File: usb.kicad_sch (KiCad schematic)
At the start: 87 parts, among them J3 PinHeader_1x3_P2.54mm_Drill1.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, J4 USB-C_Amphenol_12401598E4, J5 USB-C_Amphenol_12401598E4, J6 USB-C_Amphenol_12401598E4, U16 AP7366_SOT, U17 HD3SS3220IRNHR, U18 TPD4E05U06QDQARQ1, U19 TPD4E05U06QDQARQ1, U20 TPD4E05U06QDQARQ1, U21 USB7252C, U22 W25Q80DV_USON, U23 TPD4E05U06QDQARQ1, U24 TPD4E05U06QDQARQ1, U25 TPD4E05U06QDQARQ1, U26 TPD4E05U06QDQARQ1, U27 TPD4E05U06QDQARQ1, U28 TPD4E05U06QDQARQ1, Y2 Oscillator_25MHz_ESC_2016MV

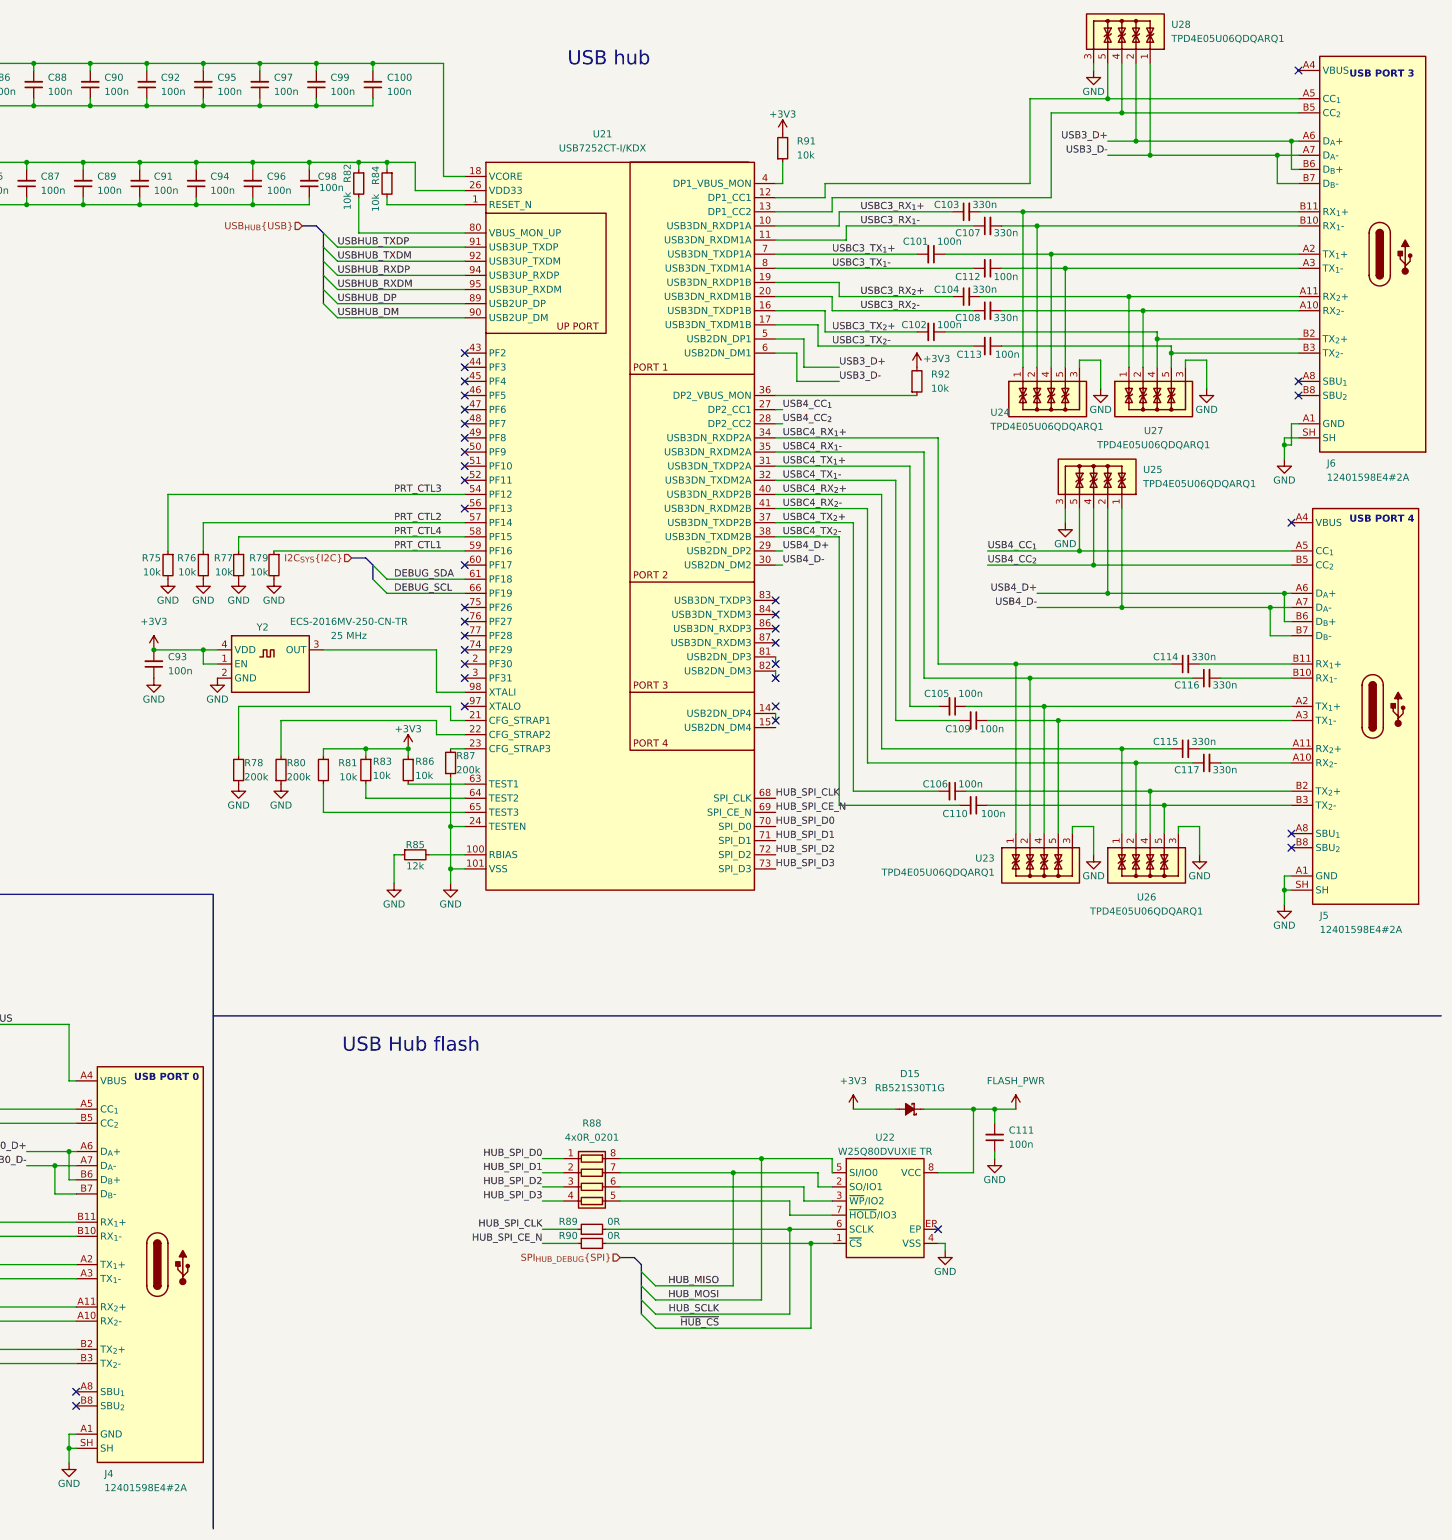
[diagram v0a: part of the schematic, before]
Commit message: [#82847] Prepare current state of schematic to merge with mockup
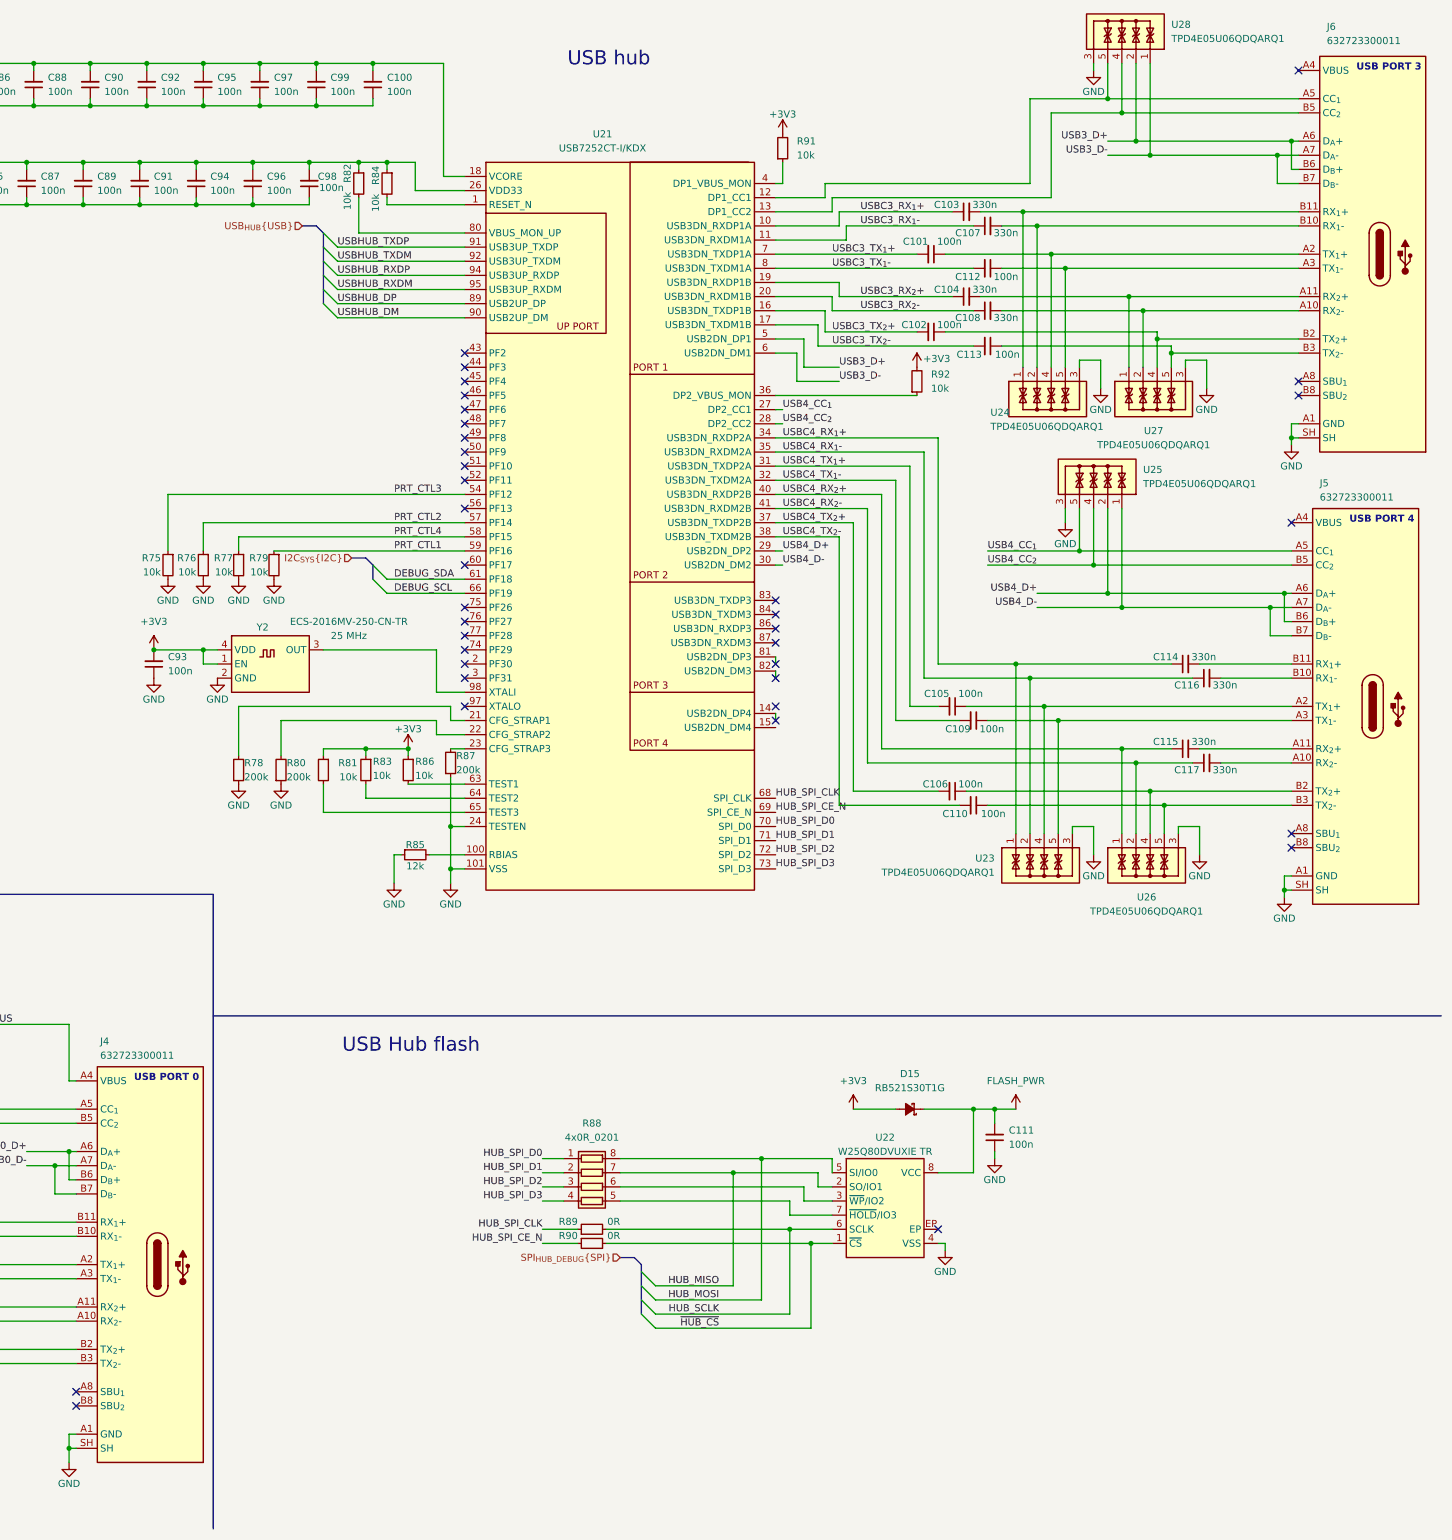
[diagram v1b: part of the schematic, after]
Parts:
- removed J4, J5, J6: USB-C_Amphenol_12401598E4, antmicro-footprints:USB-C_Receptacle_Amphenol_12401598E4, symbol antmicroUSBConnectors:USB-C_Amphenol_12401598E4
- added J4, J5, J6: USB-C_WE_632723300011, antmicro-footprints:USB-C_Receptacle_WE_632723300011, symbol antmicroUSBConnectors:USB-C_WE_632723300011
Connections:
- net GND: now also J4.A1 (GND), J4.A12 (GND), J4.B1 (GND), J4.B12 (GND), J4.SH, J5.A1 (GND), J5.A12 (GND), J5.B1 (GND), J5.B12 (GND), J5.SH, J6.A1 (GND), J6.A12 (GND), J6.B1 (GND), J6.B12 (GND), J6.SH
- net USB0_D+: now also J4.A6 (D_{A}+), J4.B6 (D_{B}+)
- net USB0_D-: now also J4.A7 (D_{A}-), J4.B7 (D_{B}-)
- net USB0_VBUS: now also J4.A4 (VBUS), J4.A9 (VBUS), J4.B4 (VBUS), J4.B9 (VBUS)
- net USB3_D+: now also J6.A6 (D_{A}+), J6.B6 (D_{B}+)
- net USB3_D-: now also J6.A7 (D_{A}-), J6.B7 (D_{B}-)
- net USB4_CC_{1}: now also J5.A5 (CC_{1})
- net USB4_CC_{2}: now also J5.B5 (CC_{2})
- net USB4_D+: now also J5.A6 (D_{A}+), J5.B6 (D_{B}+)
- net USB4_D-: now also J5.A7 (D_{A}-), J5.B7 (D_{B}-)
- net at C116.2: now also J5.B10 (RX_{1}-)
- net at C115.2: now also J5.A11 (RX_{2}+)
- net at U17.1 (CC2), U19.2, U19.9: now also J4.B5 (CC_{2})
- net at U17.2 (CC1), U19.4, U19.7: now also J4.A5 (CC_{1})
- net at C108.2, U27.2, U27.9: now also J6.A10 (RX_{2}-)
- net at U21.12 (DP1_CC1), U28.5, U28.6: now also J6.A5 (CC_{1})
- net at U21.13 (DP1_CC2), U28.4, U28.7: now also J6.B5 (CC_{2})
- net at C103.2, U24.1, U24.10: now also J6.B11 (RX_{1}+)
- net at C101.1, U24.4, U24.7: now also J6.A2 (TX_{1}+)
- net at C102.1, U27.4, U27.7: now also J6.B2 (TX_{2}+)
- net at C110.1, U26.5, U26.6: now also J5.B3 (TX_{2}-)
- net at C109.1, U23.5, U23.6: now also J5.A3 (TX_{1}-)
- net at C104.2, U27.1, U27.10: now also J6.A11 (RX_{2}+)
- net at C112.1, U24.5, U24.6: now also J6.A3 (TX_{1}-)
- net at C80.1, U18.4, U18.7: now also J4.A2 (TX_{1}+)
- net at U17.14 (RX1-), U18.1, U18.10: now also J4.B11 (RX_{1}+)
- net at U17.15 (RX1+), U18.2, U18.9: now also J4.B10 (RX_{1}-)
- net at C82.1, U18.5, U18.6: now also J4.A3 (TX_{1}-)
- net at C105.1, U23.4, U23.7: now also J5.A2 (TX_{1}+)
- net at C117.2: now also J5.A10 (RX_{2}-)
- net at C114.2: now also J5.B11 (RX_{1}+)
- net at C106.1, U26.4, U26.7: now also J5.B2 (TX_{2}+)
- net at U17.18 (RX2-), U20.1, U20.10: now also J4.A11 (RX_{2}+)
- net at U17.19 (RX2+), U20.2, U20.9: now also J4.A10 (RX_{2}-)
- net at C81.1, U20.4, U20.7: now also J4.B2 (TX_{2}+)
- net at C113.1, U27.5, U27.6: now also J6.B3 (TX_{2}-)
- net at C107.2, U24.2, U24.9: now also J6.B10 (RX_{1}-)
- net at C83.1, U20.5, U20.6: now also J4.B3 (TX_{2}-)
- new net: J6.A4 (VBUS), J6.A9 (VBUS), J6.B4 (VBUS), J6.B9 (VBUS)
- new net: J5.A4 (VBUS), J5.A9 (VBUS), J5.B4 (VBUS), J5.B9 (VBUS)

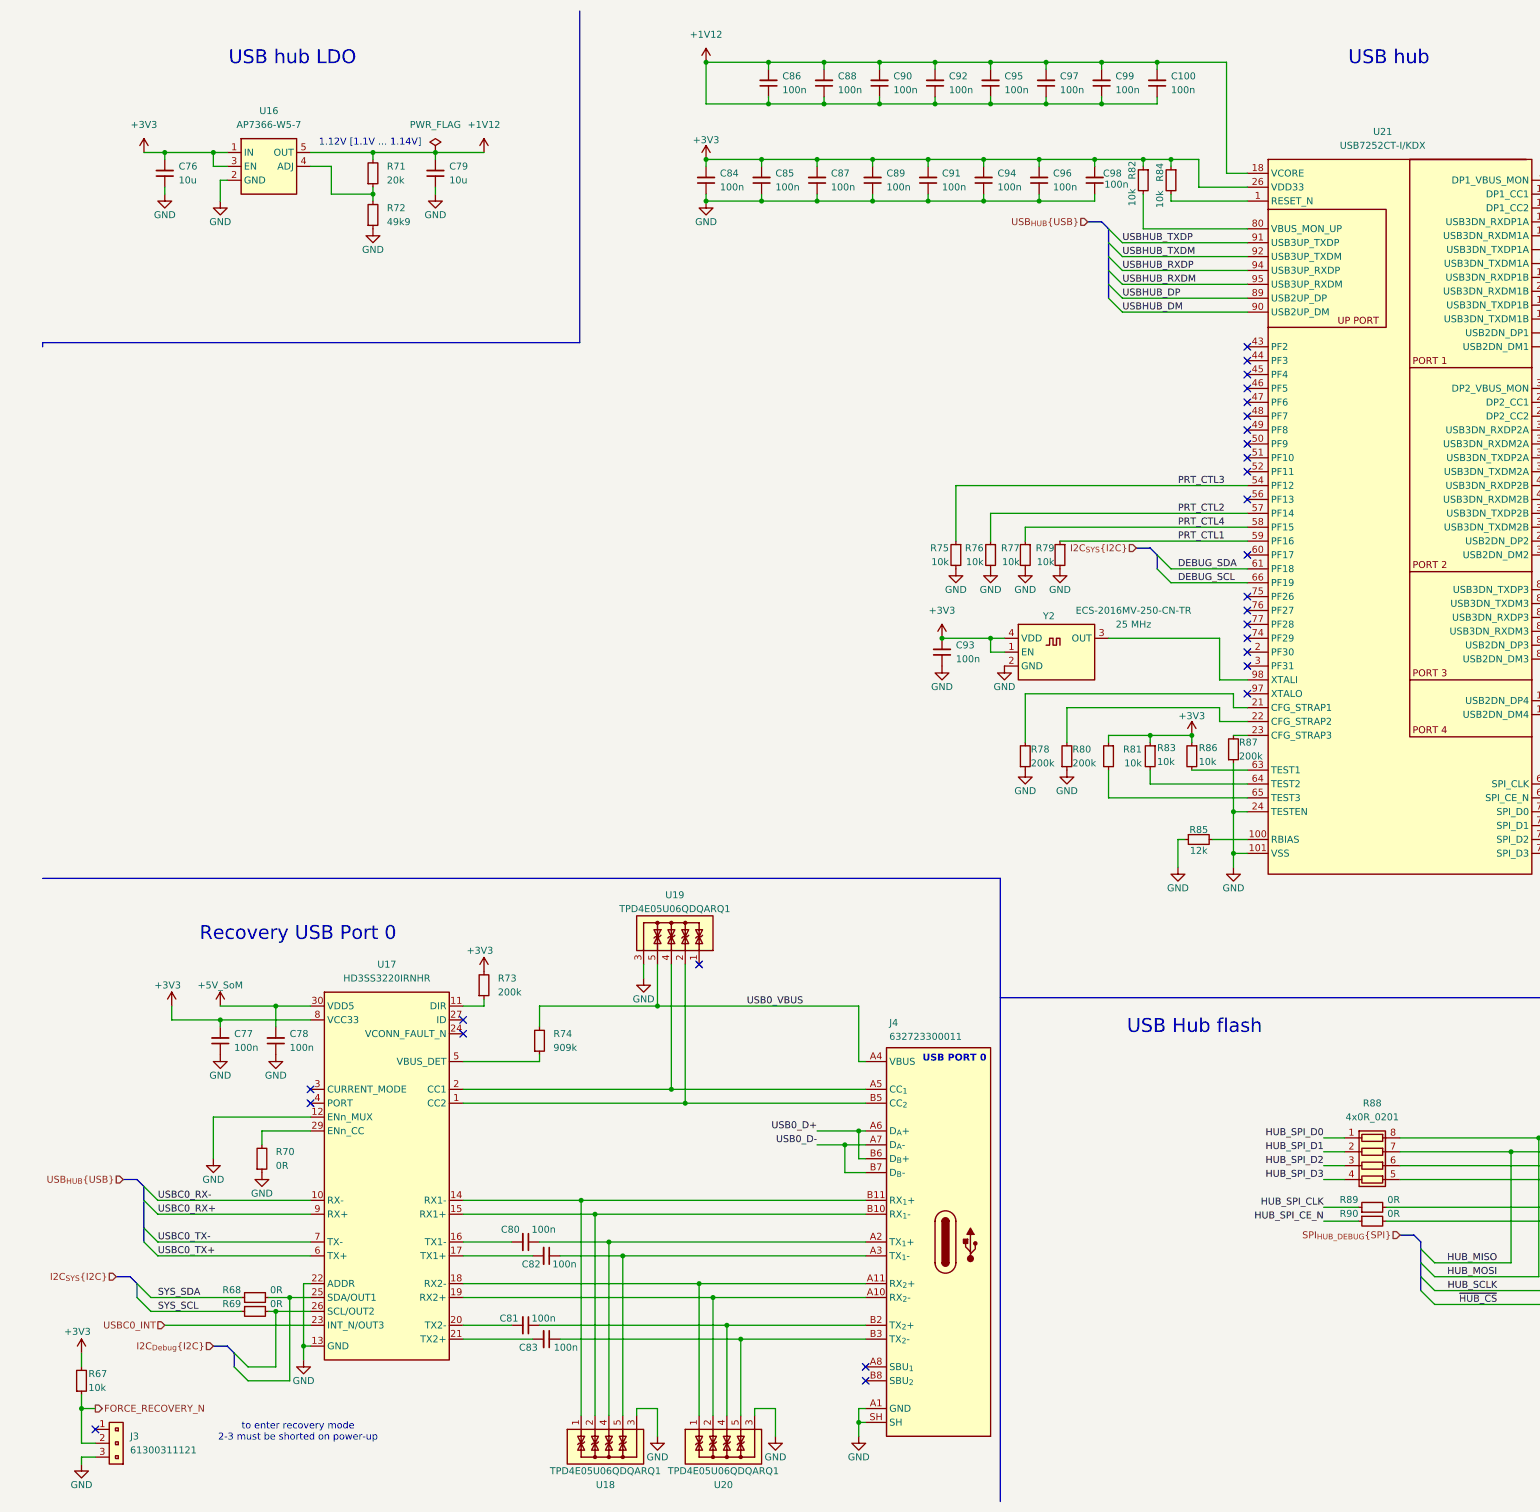
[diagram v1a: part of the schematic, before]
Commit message: [#82837] Standardise sheet sections text size
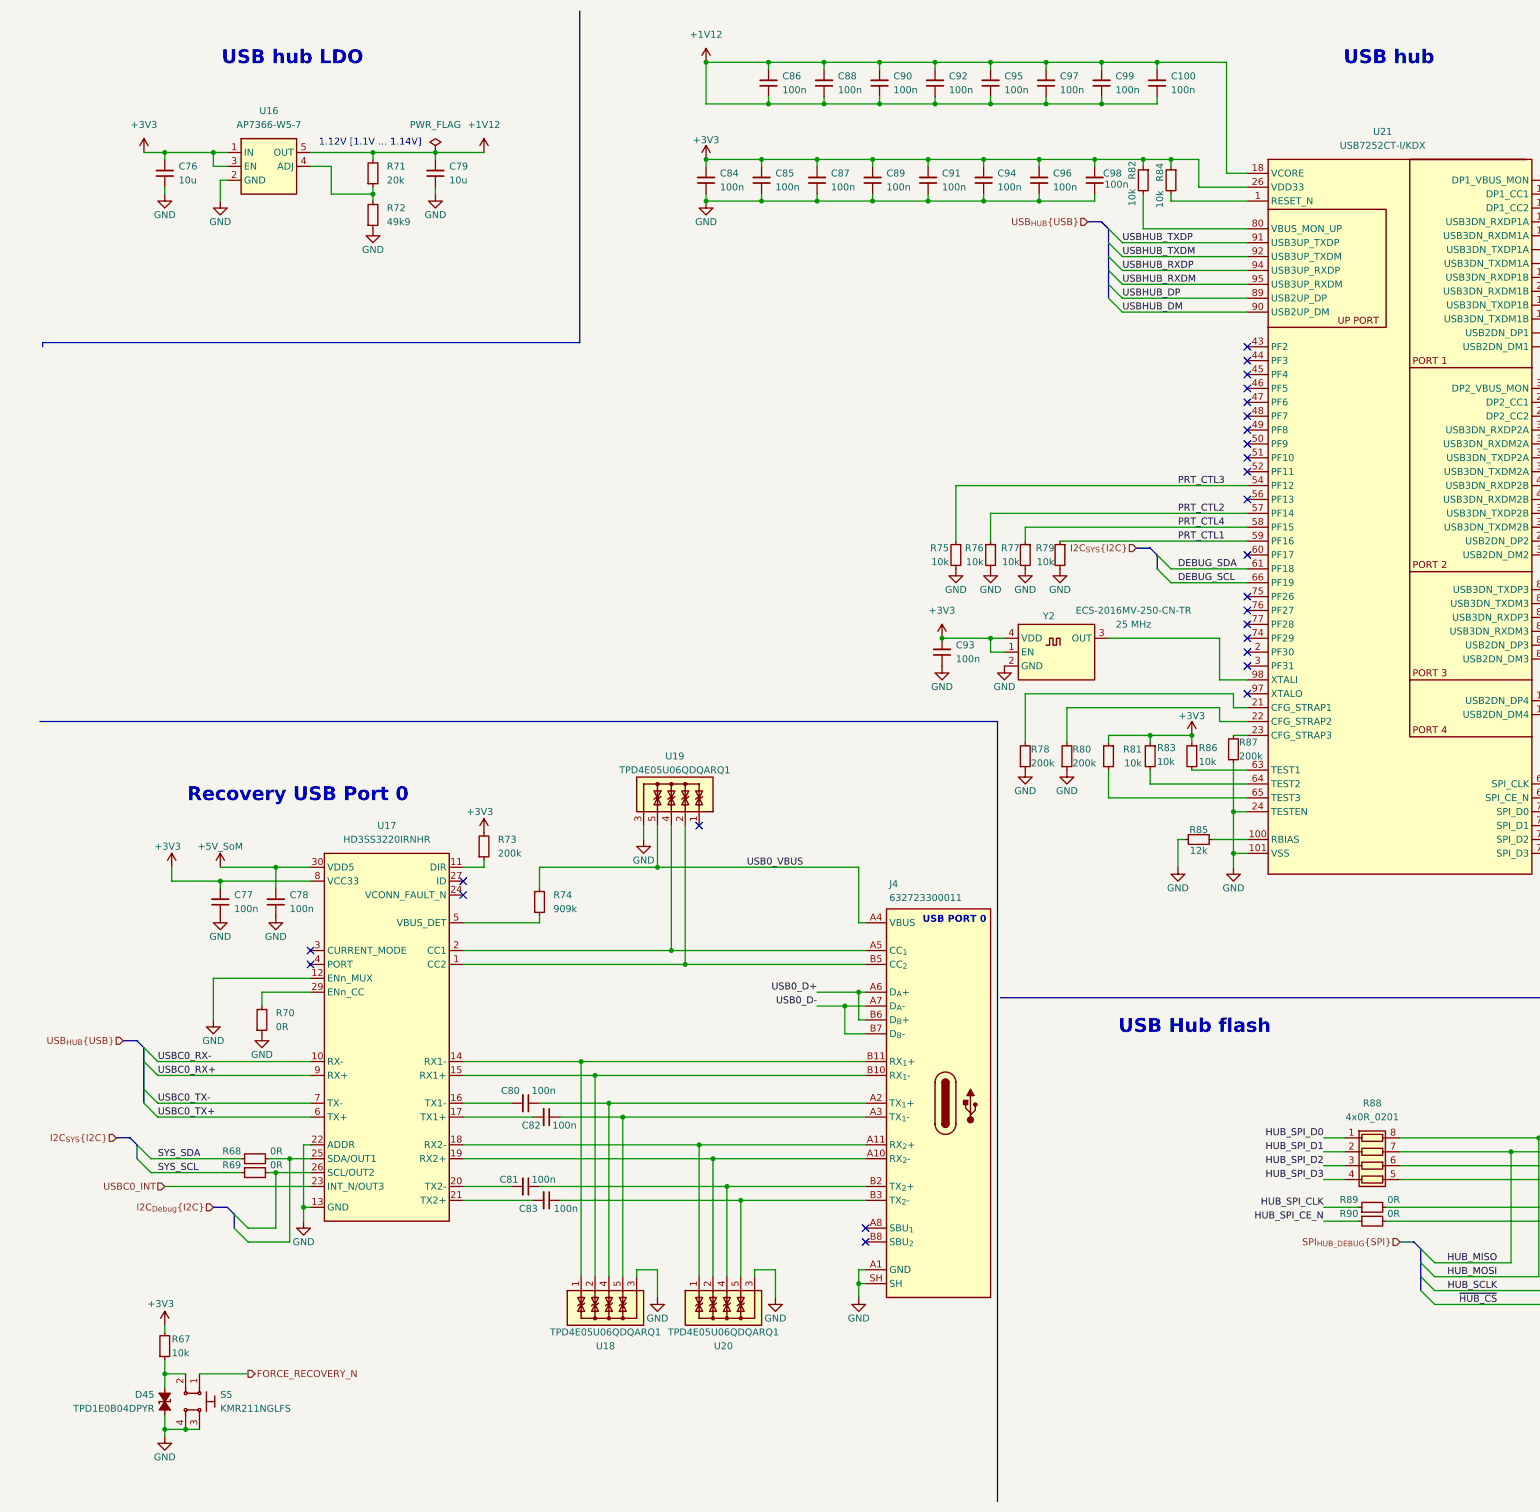
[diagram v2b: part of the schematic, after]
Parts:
- removed J3: PinHeader_1x3_P2.54mm_Drill1.1mm, antmicro-footprints:PinHeader_1x3_P2.54mm_Drill1.1mm, symbol antmicroGenericPinHeaders:PinHeader_1x3_P2.54mm_Drill1.1mm
- added D45: TPD1E0B04_XDFN-2, antmicro-footprints:XDFN-2_1x0.60mm, symbol antmicroTVSDiodes:TPD1E0B04_XDFN-2
- added S5: SW_KMR211NGLFS_SMD, antmicro-footprints:SW_KMR211NGLFS_SMD, symbol antmicroPushbuttonSwitches:SW_KMR211NGLFS_SMD
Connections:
- net FORCE_RECOVERY_N: now also S5.1; no longer R67.1
- net GND: now also D45.1 (C), S5.3, S5.4
- new net: D45.2 (A), R67.1, S5.2
- no-connect marks 42 -> 41
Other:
- note removed: "to enter recovery mode 2-3 must be shorted on power-up"
- moved on the sheet: C77, C78, C80, C81, C82, C83, J4, R67, R68, R69, R70, R73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
